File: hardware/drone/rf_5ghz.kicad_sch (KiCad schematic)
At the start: 0 parts

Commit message: Created symbol for CC3350. Almost finished schematic for OSPI
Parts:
- added U7: CC3350, Display_7Segment:CC56-12GWA, symbol SoftDrone:CC3350
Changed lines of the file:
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@@
 	(generator_version "10.0")
 	(paper "A4")
+	(symbol
+		(lib_id "SoftDrone:CC3350")
+		(at 105.41 91.44 0)
+		(unit 1)
+		(body_style 1)
+		(exclude_from_sim no)
+		(in_bom yes)
+		(on_board yes)
+		(in_pos_files yes)
+		(dnp no)
+		(fields_autoplaced yes)
+		(property "Reference" "U7"
+			(at 105.41 49.53 0)
+			(show_name no)
+			(do_not_autoplace no)
+			(effects
+				(font
+					(size 1.27 1.27)
+				)
+			)
+		)
+		(property "Value" "CC3350"
+			(at 105.41 52.07 0)
+			(show_name no)
+			(do_not_autoplace no)
+			(effects
+				(font
+					(size 1.27 1.27)
+				)
+			)
+		)
+		(property "Footprint" "Display_7Segment:CC56-12GWA"
+			(at 105.41 91.44 0)
+			(hide yes)
+			(show_name no)
+			(do_not_autoplace no)
+			(effects
+				(font
+					(size 1.27 1.27)
+				)
+			)
+		)
+		(property "Datasheet" ""
+			(at 105.41 91.44 0)
+			(hide yes)
+			(show_name no)
+			(do_not_autoplace no)
+			(effects
+				(font
+					(size 1.27 1.27)
+				)
+			)
+		)
+		(property "Description" ""
+			(at 105.41 91.44 0)
+			(hide yes)
+			(show_name no)
+			(do_not_autoplace no)
+			(effects
+				(font
+					(size 1.27 1.27)
+				)
+			)
+		)
+		(pin "10"
+		)
+		(pin "8"
+		)
+		(pin "20"
+		)
+		(pin "33"
+		)
+		(pin "37"
+		)
+		(pin "19"
+		)
+		(pin "2"
+		)
+		(pin "22"
+		)
+		(pin "3"
+		)
+		(pin "1"
+		)
+		(pin "18"
+		)
+		(pin "15"
+		)
+		(pin "21"
+		)
+		(pin "25"
+		)
+		(pin "12"
+		)
+		(pin "35"
+		)
+		(pin "5"
+		)
+		(pin "34"
+		)
+		(pin "38"
+		)
+		(pin "28"
+		)
+		(pin "31"
+		)
+		(pin "26"
+		)
+		(pin "16"
+		)
+		(pin "9"
+		)
+		(pin "6"
+		)
+		(pin "30"
+		)
+		(pin "24"
+		)
+		(pin "23"
+		)
+		(pin "41"
+		)
+		(pin "29"
+		)
+		(pin "32"
+		)
+		(pin "14"
+		)
+		(pin "7"
+		)
+		(pin "4"
+		)
+		(pin "11"
+		)
+		(pin "40"
+		)
+		(pin "39"
+		)
+		(pin "13"
+		)
+		(pin "36"
+		)
+		(pin "27"
+		)
+		(pin "17"
+		)
+		(instances
+			(project "drone"
+				(path "/62c402a6-ed3f-446b-8423-821e9cc6908b/5e69e925-338b-411d-9923-3dc150eb85e3"
+					(reference "U7")
+					(unit 1)
+				)
+			)
+		)
+	)
 )

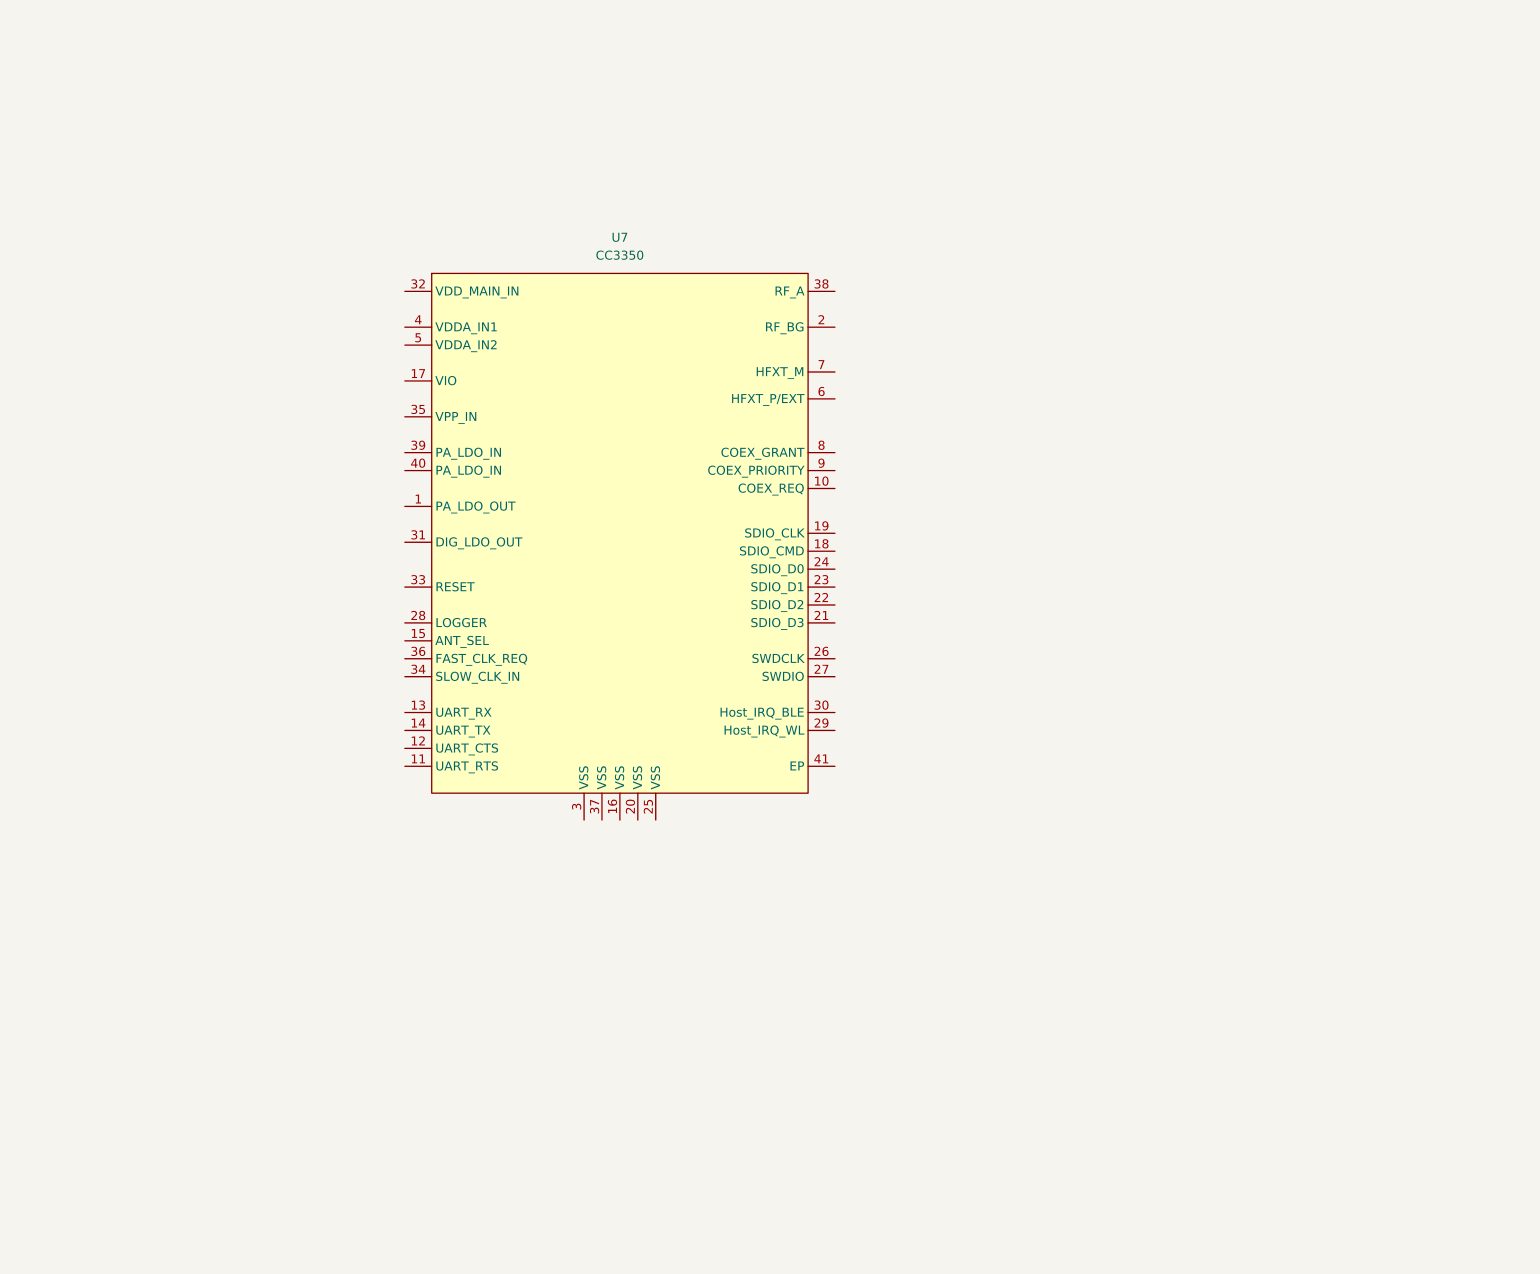
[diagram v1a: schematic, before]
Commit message: Completed rough schematic of CC3350
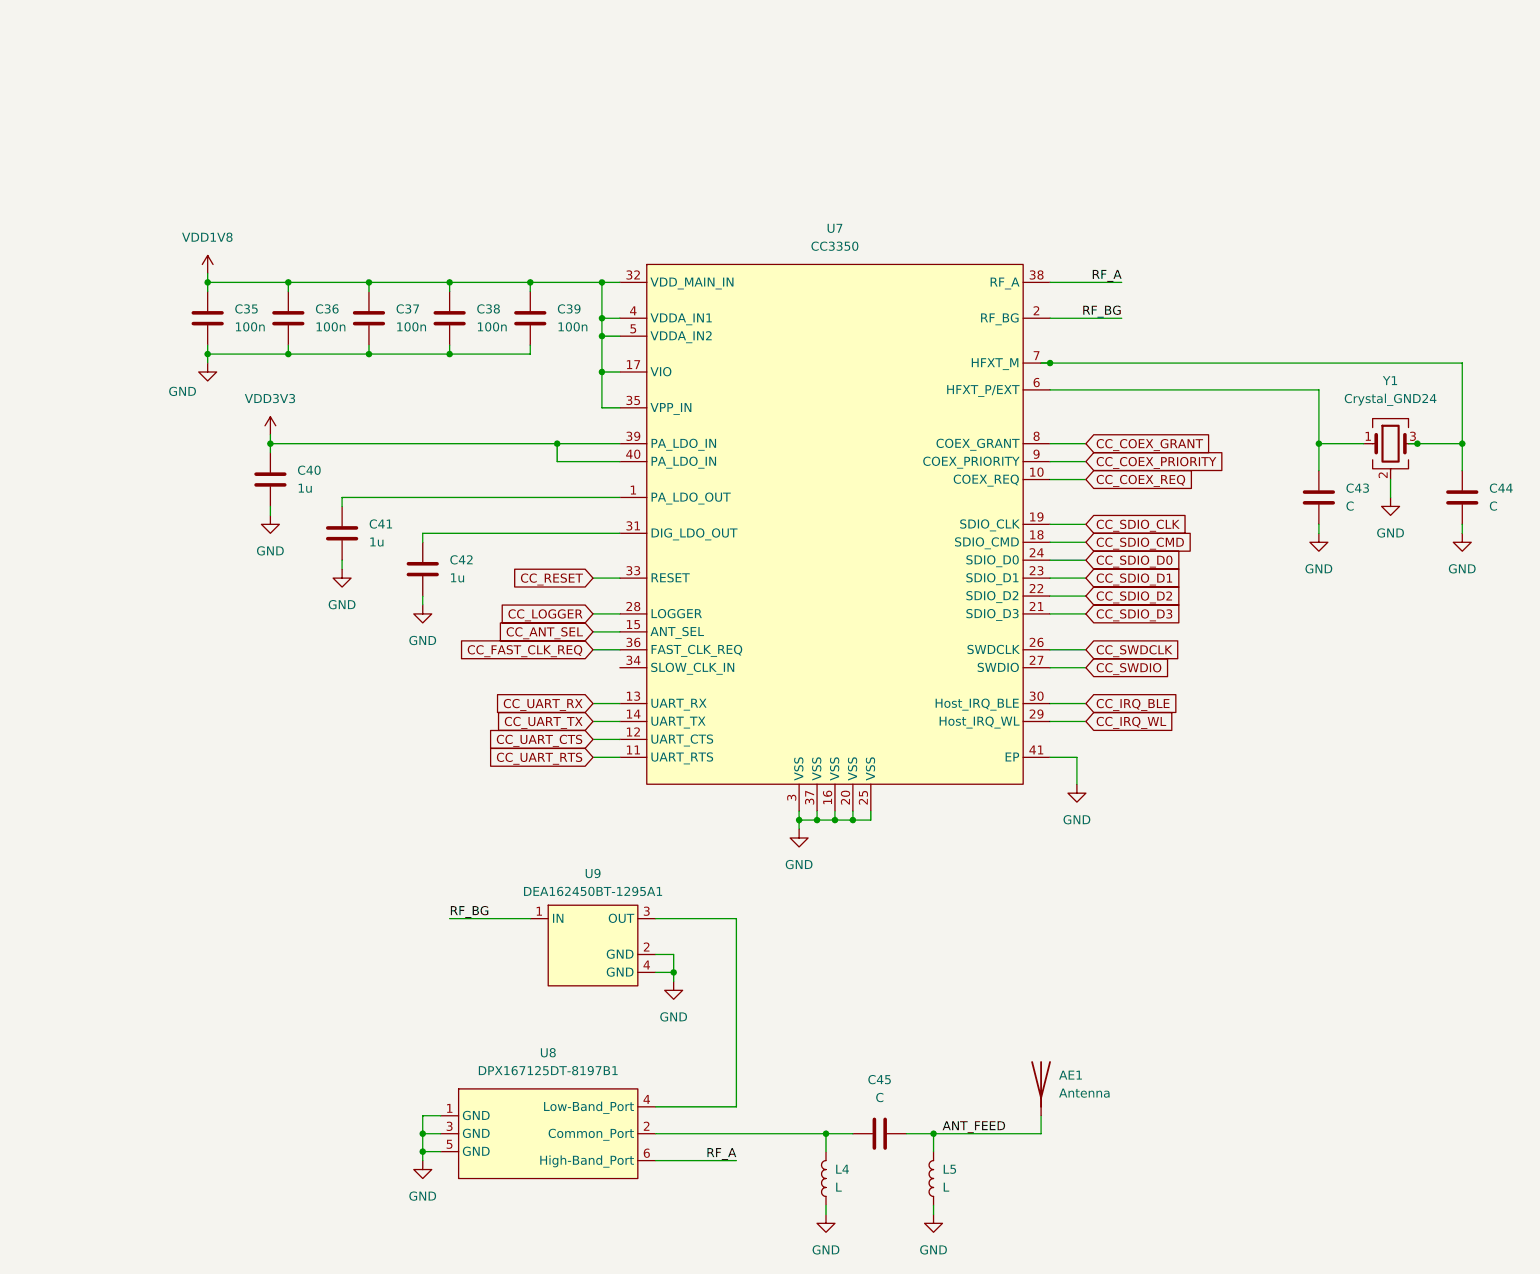
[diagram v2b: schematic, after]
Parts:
- added AE1: Antenna, Package_DFN_QFN:DFN-8-1EP_2x3mm_P0.5mm_EP0.61x2.2mm, symbol Device:Antenna
- added C35, C36, C37, C38, C39: 100n, symbol Device:C
- added C40, C41, C42: 1u, symbol Device:C
- added C43, C44, C45: C, symbol Device:C
- added L4, L5: L, symbol Device:L
- added U8: DPX167125DT-8197B1, symbol SoftDrone:DPX167125DT-8197B1
- added U9: DEA162450BT-1295A1, symbol SoftDrone:DEA162450BT-1295A1
- added Y1: Crystal_GND24, Package_DFN_QFN:DFN-6-1EP_3x2mm_P0.5mm_EP1.65x1.35mm, symbol Device:Crystal_GND24
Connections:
- net at U7.1 (PA_LDO_OUT): now also C41.1
- net CC_COEX_REQ: now reaches U7.10 (COEX_REQ)
- net CC_UART_RTS: now reaches U7.11 (UART_RTS)
- net CC_UART_CTS: now reaches U7.12 (UART_CTS)
- net CC_UART_RX: now reaches U7.13 (UART_RX)
- net CC_UART_TX: now reaches U7.14 (UART_TX)
- net CC_ANT_SEL: now reaches U7.15 (ANT_SEL)
- net GND: now reaches U7.16 (VSS)
- net GND: now also U7.20 (VSS), U7.25 (VSS), U7.3 (VSS), U7.37 (VSS), U7.41 (EP), C35.2, C36.2, C37.2, C38.2, C39.2, C40.2, C41.2, C42.2, C43.2, C44.2, L4.1, L5.1, U8.1 (GND), U8.3 (GND), U8.5 (GND), U9.2 (GND), U9.4 (GND), Y1.2 (G), Y1.4 (G)
- net VDD1V8: now reaches U7.17 (VIO)
- net VDD1V8: now also U7.32 (VDD_MAIN_IN), U7.35 (VPP_IN), U7.4 (VDDA_IN1), U7.5 (VDDA_IN2), C35.1, C36.1, C37.1, C38.1, C39.1
- net CC_SDIO_CMD: now reaches U7.18 (SDIO_CMD)
- net CC_SDIO_CLK: now reaches U7.19 (SDIO_CLK)
- net RF_BG: now reaches U7.2 (RF_BG)
- net RF_BG: now also U9.1 (IN)
- net CC_SDIO_D3: now reaches U7.21 (SDIO_D3)
- net CC_SDIO_D2: now reaches U7.22 (SDIO_D2)
- net CC_SDIO_D1: now reaches U7.23 (SDIO_D1)
- net CC_SDIO_D0: now reaches U7.24 (SDIO_D0)
- net CC_SWDCLK: now reaches U7.26 (SWDCLK)
- net CC_SWDIO: now reaches U7.27 (SWDIO)
- net CC_LOGGER: now reaches U7.28 (LOGGER)
- net CC_IRQ_WL: now reaches U7.29 (Host_IRQ_WL)
- net CC_IRQ_BLE: now reaches U7.30 (Host_IRQ_BLE)
- net at U7.31 (DIG_LDO_OUT): now also C42.1
- net CC_RESET: now reaches U7.33 (RESET)
- net CC_FAST_CLK_REQ: now reaches U7.36 (FAST_CLK_REQ)
- net RF_A: now reaches U7.38 (RF_A)
- net RF_A: now also U8.6 (High-Band_Port)
- net VDD3V3: now reaches U7.39 (PA_LDO_IN)
- net VDD3V3: now also U7.40 (PA_LDO_IN), C40.1
- net at U7.6 (HFXT_P/EXT): now also C43.1, Y1.1
- net at U7.7 (HFXT_M): now also C44.1, Y1.3
- net CC_COEX_GRANT: now reaches U7.8 (COEX_GRANT)
- net CC_COEX_PRIORITY: now reaches U7.9 (COEX_PRIORITY)
- new net: U8.4 (Low-Band_Port), U9.3 (OUT)
- new net: C45.1, L4.2, U8.2 (Common_Port)
- new net ANT_FEED: AE1.1 (A), C45.2, L5.2
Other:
- moved on the sheet: U7

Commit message: more radio work
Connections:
- net CC_SDIO_CLK renamed CC_SDMMC1_CLK
- net CC_SDIO_CMD renamed CC_SDMMC1_CMD
- net CC_SDIO_D0 renamed CC_SDMMC1_D0
- net CC_SDIO_D1 renamed CC_SDMMC1_D1
- net CC_SDIO_D2 renamed CC_SDMMC1_D2
- net CC_SDIO_D3 renamed CC_SDMMC1_D3
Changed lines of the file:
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@@
-	)
-	(junction
-		(at 166.37 67.31)
-		(diameter 0)
-		(color 0 0 0 0)
 	)
 	(junction
@@
 	(wire
 		(pts
-			(xy 165.1 67.31) (xy 166.37 67.31)
-		)
-		(stroke
-			(width 0)
-			(type default)
-		)
-	)
-	(wire
-		(pts
 			(xy 55.88 77.47) (xy 55.88 78.74)
 		)
@@
 		)
 	)
-	(global_label "CC_SDIO_D1"
+	(global_label "CC_SDMMC1_D1"
 		(shape input)
 		(at 171.45 97.79 0)
@@
 		)
 		(property "Intersheetrefs" "${INTERSHEET_REFS}"
-			(at 185.8047 97.79 0)
+			(at 189.2517 97.79 0)
 			(hide yes)
 			(show_name no)
@@
 		)
 	)
-	(global_label "CC_SDIO_D3"
+	(global_label "CC_SDMMC1_D3"
 		(shape input)
 		(at 171.45 102.87 0)
@@
 		)
 		(property "Intersheetrefs" "${INTERSHEET_REFS}"
-			(at 185.8047 102.87 0)
+			(at 189.2517 102.87 0)
 			(hide yes)
 			(show_name no)
@@
 		)
 	)
-	(global_label "CC_SDIO_D0"
+	(global_label "CC_SDMMC1_D0"
 		(shape input)
 		(at 171.45 95.25 0)
@@
 		)
 		(property "Intersheetrefs" "${INTERSHEET_REFS}"
-			(at 185.8047 95.25 0)
+			(at 189.2517 95.25 0)
 			(hide yes)
 			(show_name no)
@@
 		)
 	)
-	(global_label "CC_SDIO_CMD"
+	(global_label "CC_SDMMC1_CMD"
 		(shape input)
 		(at 171.45 92.71 0)
@@
 		)
 		(property "Intersheetrefs" "${INTERSHEET_REFS}"
-			(at 187.3166 92.71 0)
+			(at 190.7636 92.71 0)
 			(hide yes)
 			(show_name no)
@@
 		)
 	)
-	(global_label "CC_SDIO_CLK"
+	(global_label "CC_SDMMC1_CLK"
 		(shape input)
 		(at 171.45 90.17 0)
@@
 		)
 		(property "Intersheetrefs" "${INTERSHEET_REFS}"
-			(at 186.8933 90.17 0)
+			(at 190.3403 90.17 0)
 			(hide yes)
 			(show_name no)
@@
 		)
 	)
-	(global_label "CC_SDIO_D2"
+	(global_label "CC_SDMMC1_D2"
 		(shape input)
 		(at 171.45 100.33 0)
@@
 		)
 		(property "Intersheetrefs" "${INTERSHEET_REFS}"
-			(at 185.8047 100.33 0)
-			(hide yes)
-			(show_name no)
+			(at 189.2517 100.33 0)
+			(hide yes)
+			(show_name no)

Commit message: Fixed SMPS and LDO sequencing issues
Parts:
- AE1: footprint Package_DFN_QFN:DFN-8-1EP_2x3mm_P0.5mm_EP0.61x2.2mm -> (none)
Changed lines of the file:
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@@
 			)
 		)
-		(property "Footprint" "Package_DFN_QFN:DFN-8-1EP_2x3mm_P0.5mm_EP0.61x2.2mm"
+		(property "Footprint" ""
 			(at 165.1 168.91 0)
 			(hide yes)

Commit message: Finished GNSS, did more pinmuxxing
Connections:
- net ANT_FEED renamed CC_ANT_FEED
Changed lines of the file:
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@@
-	(wire
-		(pts
-			(xy 165.1 176.53) (xy 149.86 176.53)
-		)
-		(stroke
-			(width 0)
-			(type default)
-		)
-	)
 	(wire
 		(pts
@@
 		(pts
 			(xy 77.47 179.07) (xy 77.47 180.34)
+		)
+		(stroke
+			(width 0)
+			(type default)
+		)
+	)
+	(wire
+		(pts
+			(xy 149.86 176.53) (xy 165.1 176.53)
 		)
 		(stroke
@@
 		)
 	)
-	(label "ANT_FEED"
-		(at 151.13 176.53 0)
+	(label "CC_ANT_FEED"
+		(at 149.86 176.53 0)
 		(effects
 			(font
